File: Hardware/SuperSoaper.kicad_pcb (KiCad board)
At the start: 2 copper layers, 5 parts, among them U1 TPS62933, U2 TMC2209, U3 ATtiny412

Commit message: minor details changed
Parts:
- removed S1, S2: DSHP04TSGER, easyeda2kicad:SW-SMD_8P-P1.27-L7.8-W5.4
- added C1: 10u, Capacitor_SMD:C_0603_1608Metric, F.Cu at (20.7, 17.4)
- added C10: 100n, Capacitor_SMD:C_0603_1608Metric, F.Cu at (24.7, 17.4)
- added C11: 100n, Capacitor_SMD:C_0603_1608Metric, F.Cu at (24.7, 19.9)
- added C12: 100n, Capacitor_SMD:C_0603_1608Metric, F.Cu at (24.7, 22.4)
- added C13: 100u, Capacitor_SMD:C_Elec_8x10.2, F.Cu at (53.8, 21.1)
- added C14: 22n 50V, Capacitor_SMD:C_0603_1608Metric, F.Cu at (24.7, 24.9)
- added C15: 100n 16V, Capacitor_SMD:C_0603_1608Metric, F.Cu at (24.7, 27.4)
- added C16: 2u2, Capacitor_SMD:C_0603_1608Metric, F.Cu at (24.7, 29.9)
- added C17: 4u7, Capacitor_SMD:C_0603_1608Metric, F.Cu at (24.7, 32.5)
- added C2: 10u, Capacitor_SMD:C_0603_1608Metric, F.Cu at (20.7, 19.9)
- added C3: 100n, Capacitor_SMD:C_0603_1608Metric, F.Cu at (20.7, 22.4)
- added C4: 33n, Capacitor_SMD:C_0603_1608Metric, F.Cu at (20.7, 24.9)
- added C5: 100n, Capacitor_SMD:C_0603_1608Metric, F.Cu at (20.7, 27.4)
- added C6: 22n, Capacitor_SMD:C_0603_1608Metric, F.Cu at (20.7, 29.9)
- added C7: 22n, Capacitor_SMD:C_0603_1608Metric, F.Cu at (20.7, 32.5)
- added C8: 100n, Capacitor_SMD:C_0603_1608Metric, F.Cu at (20.7, 35.0)
- added C9: 10p, Capacitor_SMD:C_0603_1608Metric, F.Cu at (20.7, 37.5)
- added DC1: DC-005-5A-2.0-SMT, easyeda2kicad:DC-IN-TH_DC-005-5A-2.0-SMT, F.Cu at (43.5, 47.3)
- added J1: DC_in, easyeda2kicad:CONN-TH_B4B-XH-A-LF-SN, F.Cu at (25.5, 42.8)
- added J2: Stepper, easyeda2kicad:CONN-TH_B4B-XH-A-LF-SN, F.Cu at (25.5, 49.9)
- added J3: Sensor, easyeda2kicad:HDR-TH_3P-P2.54-H-F-W10.0-N, F.Cu at (51.7, 27.4)
- added J4: UPDI, easyeda2kicad:HDR-TH_3P-P2.54-V-F, F.Cu at (39.1, 56.6)
- added L1: 6.8uH, easyeda2kicad:IND-SMD_L4.5-W4.0_SCD0403T, F.Cu at (27.4, 55.7)
- added R1: 511k, Resistor_SMD:R_0603_1608Metric, F.Cu at (24.7, 35.0)
- added R10: 10k, Resistor_SMD:R_0603_1608Metric, F.Cu at (28.7, 29.9)
- added R11: 10k, Resistor_SMD:R_0603_1608Metric, F.Cu at (28.7, 32.5)
- added R12: 10k, Resistor_SMD:R_0603_1608Metric, F.Cu at (28.7, 35.0)
- added R13: 10k, Resistor_SMD:R_0603_1608Metric, F.Cu at (28.7, 37.5)
- added R14: 4k7, Resistor_SMD:R_0603_1608Metric, F.Cu at (32.7, 17.4)
- added R15: 8k5, Resistor_SMD:R_0603_1608Metric, F.Cu at (32.7, 19.9)
- added R16: 1k5, Resistor_SMD:R_0603_1608Metric, F.Cu at (32.7, 22.4)
- added R17: 0, Resistor_SMD:R_0603_1608Metric, F.Cu at (32.7, 24.9)
- added R18: 0, Resistor_SMD:R_0603_1608Metric, F.Cu at (32.7, 27.4)
- added R2: 88k7, Resistor_SMD:R_0603_1608Metric, F.Cu at (24.7, 37.5)
- added R3: 0, Resistor_SMD:R_0603_1608Metric, F.Cu at (28.7, 17.4)
- added R4: 0, Resistor_SMD:R_0603_1608Metric, F.Cu at (28.7, 19.9)
- added R5: 49R9, Resistor_SMD:R_0603_1608Metric, F.Cu at (28.7, 22.4)
- added R6: 53k6, Resistor_SMD:R_0603_1608Metric, F.Cu at (28.7, 24.9)
- added R7: 10k2, Resistor_SMD:R_0603_1608Metric, F.Cu at (28.7, 27.4)
- added R8: 180m 1W, Resistor_SMD:R_1206_3216Metric, F.Cu at (21.5, 54.5)
- added R9: 180m 1W, Resistor_SMD:R_1206_3216Metric, F.Cu at (21.5, 57.8)
- added SW1: A6S-4101-H, easyeda2kicad:SW-SMD_8P-L11.1-W6.2-P2.54-LS9.8, F.Cu at (40.9, 22.1)
- added SW2: A6S-4101-H, easyeda2kicad:SW-SMD_8P-L11.1-W6.2-P2.54-LS9.8, F.Cu at (40.9, 34.0)
- added U4: LM358DR, Package_SO:SOIC-8_3.9x4.9mm_P1.27mm, F.Cu at (55.4, 49.6)
- U1: value TPS62933 -> TPS62933DRLR
- U2: value TMC2209 -> TMC2209-LA
- U3: value ATtiny412 -> ATtiny2X2
- moved U3 38.4 mm to (55.4, 43.2)
- moved U1 35.8 mm to (45.1, 56.5)
- moved U2 35.2 mm to (54.6, 56.3)
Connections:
- U3 pad 2: Sense -> Sensor
- U3 pad 6: Net-(S1-A1) -> UPDI

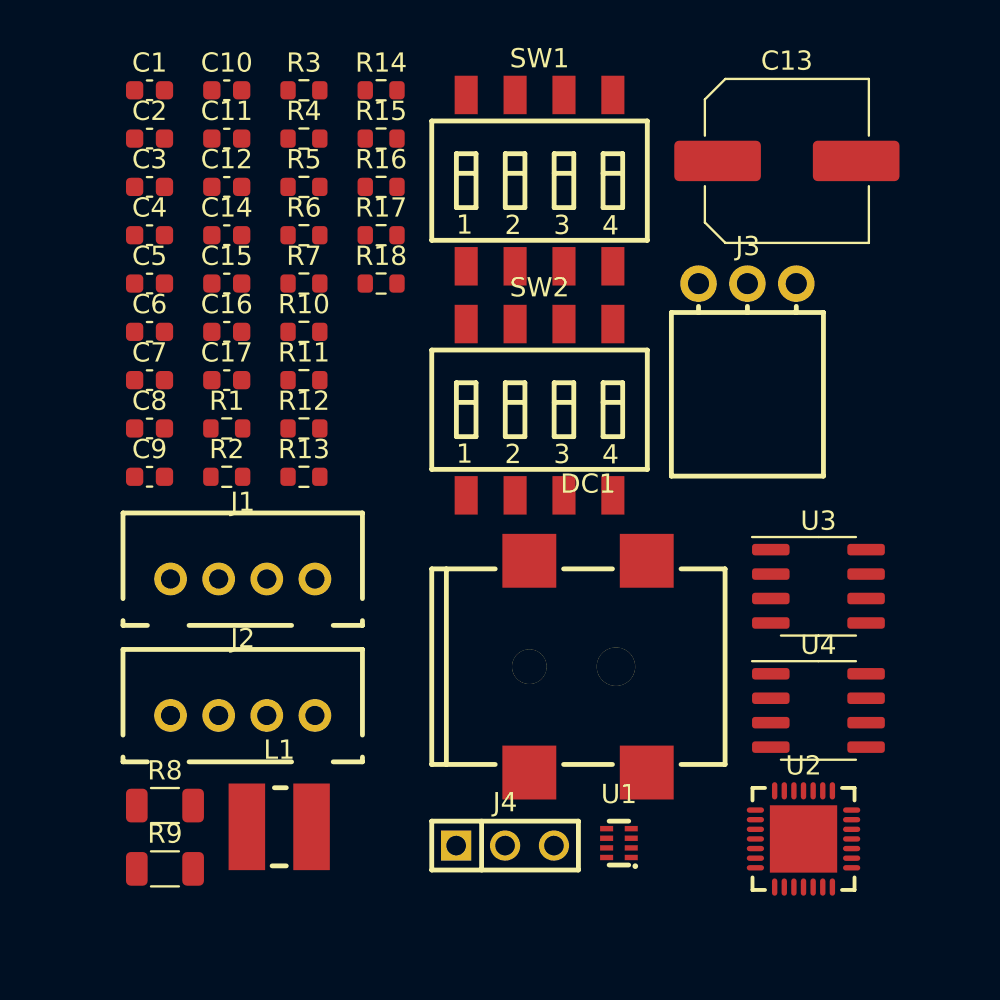
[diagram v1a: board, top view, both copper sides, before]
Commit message: CHanged from ATtiny 2X2 to STM32C011F4P6
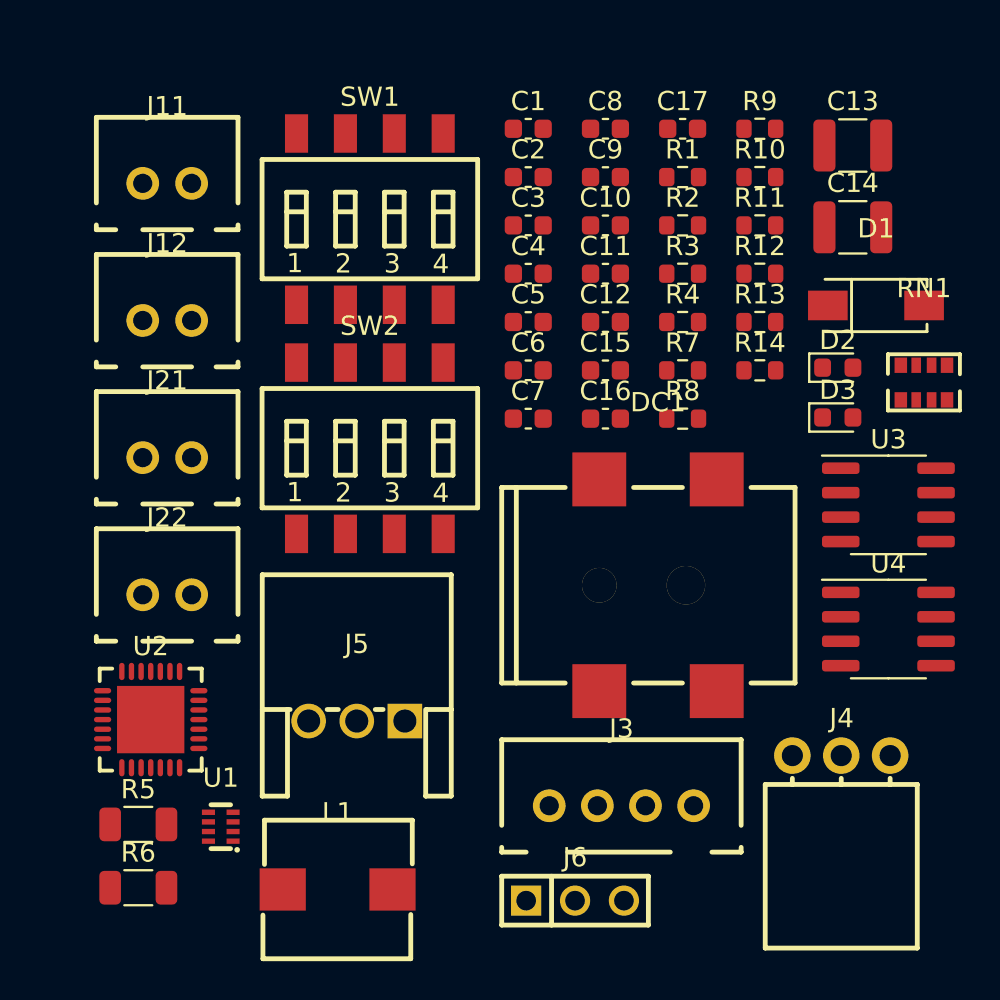
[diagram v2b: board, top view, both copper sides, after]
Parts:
- removed J1: DC_in, easyeda2kicad:CONN-TH_B4B-XH-A-LF-SN
- removed J2: Stepper, easyeda2kicad:CONN-TH_B4B-XH-A-LF-SN
- removed R15: 8k5, Resistor_SMD:R_0603_1608Metric
- removed R16: 1k5, Resistor_SMD:R_0603_1608Metric
- removed R17, R18: 0, Resistor_SMD:R_0603_1608Metric
- added D1: SS54, easyeda2kicad:SMA_L4.4-W2.8-LS5.4-R-RD, F.Cu at (58.4, 28.6)
- added D2: LED_G, LED_SMD:LED_0603_1608Metric, F.Cu at (56.4, 31.8)
- added D3: LED_R, LED_SMD:LED_0603_1608Metric, F.Cu at (56.4, 34.4)
- added J11: DC_in, easyeda2kicad:CONN-TH_B2B-XH-A-LF-SN, F.Cu at (21.6, 22.2)
- added J12: DC_in, easyeda2kicad:CONN-TH_B2B-XH-A-LF-SN, F.Cu at (21.6, 29.4)
- added J21: DC_out, easyeda2kicad:CONN-TH_B2B-XH-A-LF-SN, F.Cu at (21.6, 36.5)
- added J22: DC_out, easyeda2kicad:CONN-TH_B2B-XH-A-LF-SN, F.Cu at (21.6, 43.6)
- added J5: Sensor JST, easyeda2kicad:CONN-TH_S3B-XH-A-1-LF-SN, F.Cu at (31.4, 50.2)
- added J6: UPDI, easyeda2kicad:HDR-TH_3P-P2.54-V-F, F.Cu at (42.8, 59.5)
- added RN1: 4 x 10k, easyeda2kicad:RES-ARRAY-SMD_0603-8P-L3.2-W1.6-BL, F.Cu at (60.9, 32.6)
- C1, C2: value 10u -> 10u 50V
- C10, C11, C12, C3: value 100n -> 100n 50V
- C13: value 100u -> 10u 50V; footprint Capacitor_SMD:C_Elec_8x10.2 -> Capacitor_SMD:C_1210_3225Metric
- C14: value 22n 50V -> 10u 50V; footprint Capacitor_SMD:C_0603_1608Metric -> Capacitor_SMD:C_1210_3225Metric
- C15: value 100n 16V -> 100n 50V
- C16: value 2u2 -> 2u2 50V
- C4: value 33n -> 33n 50V
- C6, C7: value 22n -> 22u
- C9: value 10p -> 22n 50V
- J3: value Sensor -> Stepper; footprint easyeda2kicad:HDR-TH_3P-P2.54-H-F-W10.0-N -> easyeda2kicad:CONN-TH_B4B-XH-A-LF-SN
- J4: value UPDI -> Sensor; footprint easyeda2kicad:HDR-TH_3P-P2.54-V-F -> easyeda2kicad:HDR-TH_3P-P2.54-H-F-W10.0-N
- L1: footprint easyeda2kicad:IND-SMD_L4.5-W4.0_SCD0403T -> easyeda2kicad:IND-SMD_L7.4-W7.0
- R1: value 511k -> 62k
- R10: value 10k -> 8k5
- R11: value 10k -> 1k5
- R12, R13: value 10k -> 0
- R14: value 4k7 -> 10k
- R2: value 88k7 -> 10k
- R3: value 0 -> 30k9
- R4: value 0 -> 220
- R5: value 49R9 -> 180m 1W; footprint Resistor_SMD:R_0603_1608Metric -> Resistor_SMD:R_1206_3216Metric
- R6: value 53k6 -> 180m 1W; footprint Resistor_SMD:R_0603_1608Metric -> Resistor_SMD:R_1206_3216Metric
- R7: value 10k2 -> 100k
- R8: value 180m 1W -> 220; footprint Resistor_SMD:R_1206_3216Metric -> Resistor_SMD:R_0603_1608Metric
- R9: value 180m 1W -> 4k7; footprint Resistor_SMD:R_1206_3216Metric -> Resistor_SMD:R_0603_1608Metric
- moved R9 49.3 mm to (52.4, 19.4)
- moved R6 35.0 mm to (20.1, 58.8)
- moved U2 34.5 mm to (20.7, 50.1)
- moved R5 34.2 mm to (20.1, 55.5)
- moved R8 33.6 mm to (48.4, 34.5)
- moved C14 32.5 mm to (57.2, 24.5)
- moved C8 28.3 mm to (44.4, 19.4)
- moved C9 28.3 mm to (44.4, 21.9)
- moved J3 27.9 mm to (45.2, 54.6)
- moved C17 27.0 mm to (48.4, 19.4)
- moved R1 27.0 mm to (48.4, 21.9)
- moved R2 27.0 mm to (48.4, 24.4)
- moved R10 25.0 mm to (52.4, 21.9)
- moved R11 25.0 mm to (52.4, 24.4)
- moved R12 25.0 mm to (52.4, 26.9)
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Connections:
- C14 pad 1: Net-(U2-CPI) -> VCC
- C14 pad 2: Net-(U2-CPO) -> GND
- C5 pad 1: Net-(C5-Pad1) -> Net-(U1-BST)
- C9 pad 1: Net-(U1-FB) -> Net-(U2-CPI)
- C9 pad 2: Net-(C9-Pad2) -> Net-(U2-CPO)
- DC1 pad 1: VCC -> Net-(D1-A)
- J3 pad 1: +3.3V -> OA1
- J3 pad 2: GND -> OA2
- J3 pad 3: Sensor -> OB1
- J4 pad 2: UPDI -> GND
- J4 pad 3: GND -> Sensor
- R1 pad 1: VCC -> GND
- R1 pad 2: Net-(U1-EN) -> Net-(U1-RT)
- R10 pad 1: MS1 -> +3.3V
- R10 pad 2: GND -> Net-(U4-1IN+)
- R11 pad 1: MS2 -> Net-(U4-1IN+)
- R12 pad 1: DIR -> Enable
- R12 pad 2: GND -> Net-(U4-1OUT)
- R13 pad 1: SPREAD -> Enable
- R14 pad 1: STEP -> +3.3V
- R14 pad 2: Net-(U4-1IN-) -> Enable
- R2 pad 1: Net-(U1-EN) -> Net-(U1-FB)
- R3 pad 1: GND -> +3.3V
- R3 pad 2: Net-(U1-RT) -> Net-(U1-FB)
- R4 pad 1: Net-(U1-BST) -> +3.3V
- R4 pad 2: Net-(C5-Pad1) -> Net-(D2-A)
- R5 pad 1: +3.3V -> BrakeA
- R5 pad 2: Net-(C9-Pad2) -> GND
- R6 pad 1: Net-(C9-Pad2) -> GND
- R6 pad 2: Net-(U1-FB) -> BrakeB
- R7 pad 1: Net-(U1-FB) -> Net-(U2-STDBY)
- R8 pad 1: BrakeA -> Net-(D3-A)
- R8 pad 2: GND -> Net-(U2-DIAG)
- R9 pad 1: GND -> STEP
- R9 pad 2: BrakeB -> Net-(U4-1IN-)
- U1 pad 2: Net-(U1-EN) -> unconnected-(U1-EN-Pad2)
- U2 pad 11: unconnected-(U2-DIAG-Pad11) -> Net-(U2-DIAG)
- U2 pad 20: unconnected-(U2-STDBY-Pad20) -> Net-(U2-STDBY)

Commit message: Changed from ATtiny 2X2 to STM32C011F4P6
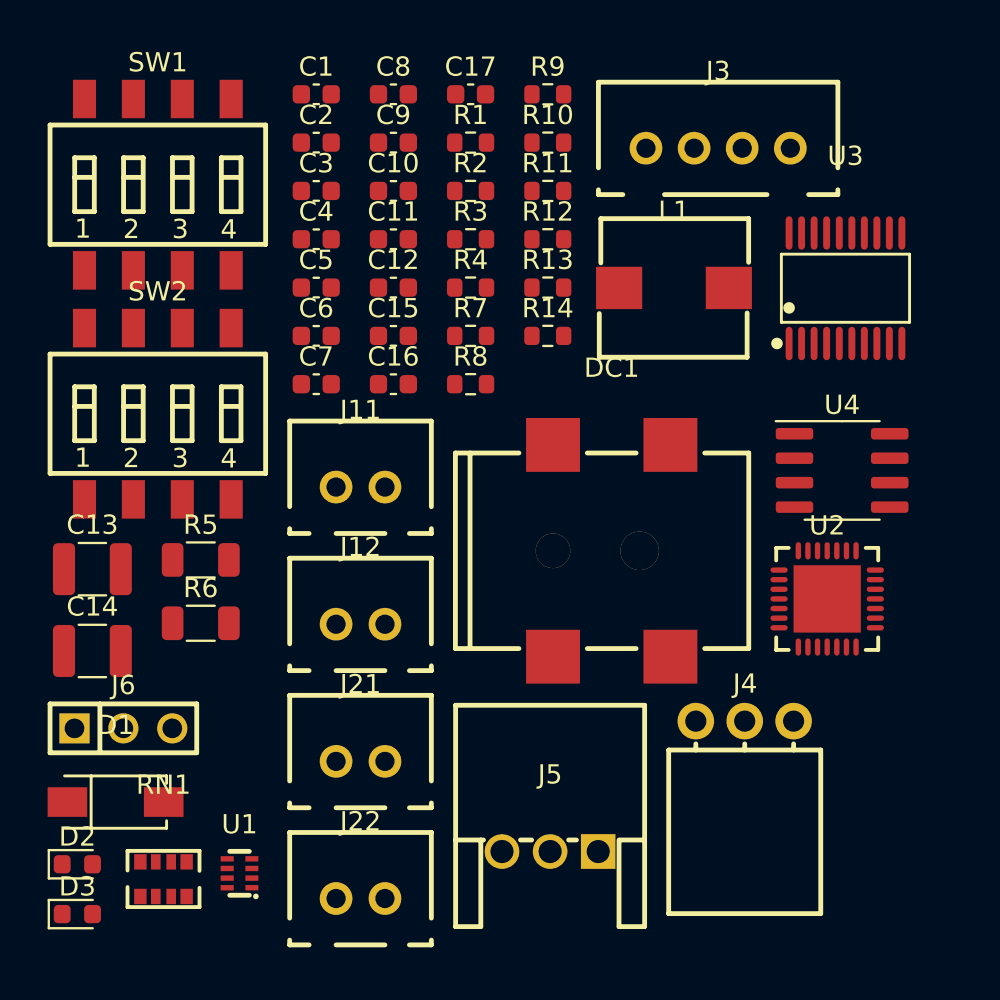
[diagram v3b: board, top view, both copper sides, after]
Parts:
- U3: value ATtiny2X2 -> STM32C011F4P6; footprint Package_SO:SOIC-8_3.9x4.9mm_P1.27mm -> easyeda2kicad:TSSOP-20_L6.5-W4.4-P0.65-LS6.4-BL
- moved D2 47.2 mm to (16.9, 57.6)
- moved RN1 47.2 mm to (21.4, 58.4)
- moved D1 47.2 mm to (18.9, 54.4)
- moved D3 47.2 mm to (16.9, 60.2)
- moved C13 45.2 mm to (17.7, 42.3)
- moved C14 45.2 mm to (17.7, 46.5)
- moved L1 35.8 mm to (47.9, 27.7)
- moved U2 35.7 mm to (55.9, 43.8)
- moved J3 34.5 mm to (50.2, 20.4)
- moved J6 25.1 mm to (19.3, 50.5)
- moved J11 18.7 mm to (31.6, 38.0)
- moved J12 18.7 mm to (31.6, 45.1)
- moved J21 18.7 mm to (31.6, 52.3)
- moved J22 18.7 mm to (31.6, 59.4)
- moved R5 14.1 mm to (23.3, 41.8)
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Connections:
- J6 pad 2: UPDI -> unconnected-(J6-Pin_2-Pad2)
- SW2 pad 1: UPDI -> unconnected-(SW2-A1-Pad1)
- SW2 pad 2: Net-(SW2-A2) -> unconnected-(SW2-A2-Pad2)
- SW2 pad 3: Net-(SW2-A3) -> unconnected-(SW2-A3-Pad3)
- SW2 pad 4: Net-(SW2-A4) -> unconnected-(SW2-A4-Pad4)
- U3 pad 1: +3.3V -> unconnected-(U3-PB7-Pad1)
- U3 pad 2: Sensor -> unconnected-(U3-PC14-OSCX_IN-Pad2)
- U3 pad 3: STEP -> unconnected-(U3-PC15-OSCX_OUT-Pad3)
- U3 pad 4: Net-(SW2-A2) -> unconnected-(U3-VDD/VDDA-Pad4)
- U3 pad 5: Net-(SW2-A3) -> unconnected-(U3-VSS/VSSA-Pad5)
- U3 pad 6: UPDI -> unconnected-(U3-PF2-NRST-Pad6)
- U3 pad 7: Net-(SW2-A4) -> unconnected-(U3-PA0-Pad7)
- U3 pad 8: GND -> unconnected-(U3-PA1-Pad8)
